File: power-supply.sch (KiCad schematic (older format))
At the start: 16 parts, among them J13 USB_A, U11 BA33BC0FP-E2, U13 LM2990SX-5.0, U14 BA50BC0FP-E2

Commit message: Minor fixes and cleanups
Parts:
- C18: value 22uF -> 330uF/LOW_ESR; footprint Capacitor_SMD:CP_Elec_6.3x5.4 -> Capacitor_SMD:CP_Elec_6.3x7.7
- C19, C25, C28: value 1uF -> 10uF
- C24: value 33uF/LOW_ESR -> 100uF
- C26: footprint Capacitor_SMD:CP_Elec_6.3x5.4 -> Capacitor_SMD:CP_Elec_6.3x7.7
- C29: footprint Capacitor_SMD:CP_Elec_6.3x5.4 -> Capacitor_SMD:CP_Elec_6.3x5.8
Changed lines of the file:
@@
 P 1950 3700
 F 0 "C19" H 1960 3770 50  0000 L CNN
-F 1 "1uF" H 1960 3620 50  0000 L CNN
+F 1 "10uF" H 1960 3620 50  0000 L CNN
 F 2 "Capacitor_SMD:C_0805_2012Metric_Pad1.18x1.45mm_HandSolder" H 1950 3700 50  0001 C CNN
 F 3 "" H 1950 3700 50  0001 C CNN
@@
 P 2750 3700
 F 0 "C18" H 2838 3746 50  0000 L CNN
-F 1 "22uF" H 2838 3655 50  0000 L CNN
-F 2 "Capacitor_SMD:CP_Elec_6.3x5.4" H 2750 3700 50  0001 C CNN
+F 1 "330uF/LOW_ESR" H 2838 3655 50  0000 L CNN
+F 2 "Capacitor_SMD:CP_Elec_6.3x7.7" H 2750 3700 50  0001 C CNN
 F 3 "~" H 2750 3700 50  0001 C CNN
 	1    2750 3700
@@
 F 0 "C26" H 9688 4246 50  0000 L CNN
 F 1 "330uF/LOW_ESR" H 9688 4155 50  0000 L CNN
-F 2 "Capacitor_SMD:CP_Elec_6.3x5.4" H 9600 4200 50  0001 C CNN
+F 2 "Capacitor_SMD:CP_Elec_6.3x7.7" H 9600 4200 50  0001 C CNN
 F 3 "~" H 9600 4200 50  0001 C CNN
 	1    9600 4200
@@
 P 4250 3550
 F 0 "C24" V 4350 3500 50  0000 L CNN
-F 1 "33uF/LOW_ESR" V 4450 3100 50  0000 L CNN
+F 1 "100uF" V 4150 3450 50  0000 L CNN
 F 2 "Capacitor_SMD:CP_Elec_6.3x5.4" H 4250 3550 50  0001 C CNN
 F 3 "~" H 4250 3550 50  0001 C CNN
@@
 F 0 "C29" H 8288 4346 50  0000 L CNN
 F 1 "330uF/LOW_ESR" H 8288 4255 50  0000 L CNN
-F 2 "Capacitor_SMD:CP_Elec_6.3x5.4" H 8200 4300 50  0001 C CNN
+F 2 "Capacitor_SMD:CP_Elec_6.3x5.8" H 8200 4300 50  0001 C CNN
 F 3 "~" H 8200 4300 50  0001 C CNN
 	1    8200 4300
@@
 P 8800 4200
 F 0 "C25" H 8810 4270 50  0000 L CNN
-F 1 "1uF" H 8810 4120 50  0000 L CNN
+F 1 "10uF" H 8810 4120 50  0000 L CNN
 F 2 "Capacitor_SMD:C_0805_2012Metric_Pad1.18x1.45mm_HandSolder" H 8800 4200 50  0001 C CNN
 F 3 "" H 8800 4200 50  0001 C CNN
@@
 P 7200 4300
 F 0 "C28" H 7210 4370 50  0000 L CNN
-F 1 "1uF" H 7210 4220 50  0000 L CNN
+F 1 "10uF" H 7210 4220 50  0000 L CNN
 F 2 "Capacitor_SMD:C_0805_2012Metric_Pad1.18x1.45mm_HandSolder" H 7200 4300 50  0001 C CNN
 F 3 "" H 7200 4300 50  0001 C CNN

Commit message: Onboard FPGA, passthroughs and a lot of other stuff
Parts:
- removed J13: USB_A, Connector_USB:USB_A_Molex_67643_Horizontal, symbol Connector:USB_A
- added C30, C31, C32, C33, C34, C35, C36, C37, C38, C39: 0.1uF, Capacitor_SMD:C_0603_1608Metric_Pad1.08x0.95mm_HandSolder, symbol bkm-68x-simple-rescue:C_Small
- added C56, C57, C59: 0.1uF, Capacitor_SMD:C_0805_2012Metric_Pad1.18x1.45mm_HandSolder, symbol bkm-68x-simple-rescue:C_Small
- added C58: 100uF, Capacitor_SMD:CP_Elec_6.3x5.4, symbol Device:CP_Small
- added U15: 10M08SC, Package_QFP:EQFP-144-1EP_20x20mm_P0.5mm_EP8.93x8.7mm_ThermalVias, symbol bkm-68x-simple-rescue:10M08SC-FPGA_Intel
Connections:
- wire segments 53 -> 84
- no-connect marks 2 -> 0
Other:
- moved on the sheet: C14, C15, C16, C17, C18, C19, C23, C24, U11

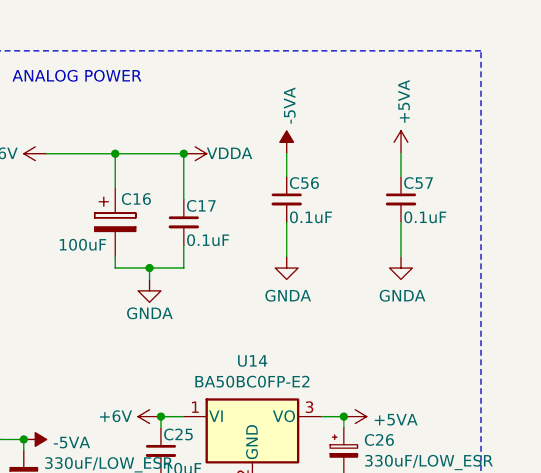
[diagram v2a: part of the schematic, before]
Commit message: Replace ADG1611BRUZ with BCPZ
Should also be compatible with Vishay DG1411EEN-T1-GE4
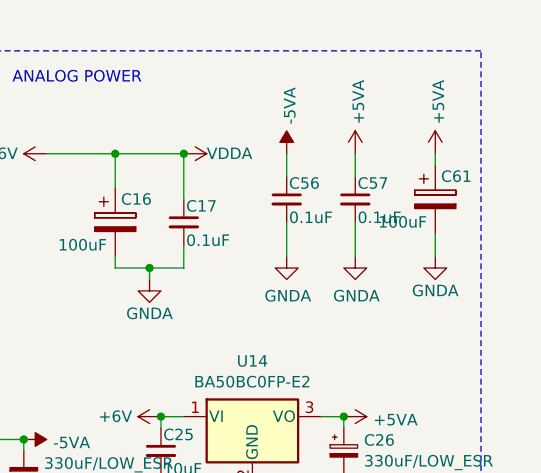
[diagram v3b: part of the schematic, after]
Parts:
- added C61: 100uF, Capacitor_SMD:CP_Elec_6.3x5.3, symbol bkm-68x-simple-rescue:CP
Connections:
- net +5VA: now also C61.1
- net GNDA: now also C61.2
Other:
- moved on the sheet: C57
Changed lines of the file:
@@
 L bkm-68x-simple-rescue:C_Small C57
 U 1 1 60B680F3
-P 9850 3100
-F 0 "C57" H 9860 3170 50  0000 L CNN
-F 1 "0.1uF" H 9860 3020 50  0000 L CNN
-F 2 "Capacitor_SMD:C_0805_2012Metric_Pad1.18x1.45mm_HandSolder" H 9850 3100 50  0001 C CNN
-F 3 "" H 9850 3100 50  0001 C CNN
-	1    9850 3100
+P 9650 3100
+F 0 "C57" H 9660 3170 50  0000 L CNN
+F 1 "0.1uF" H 9660 3020 50  0000 L CNN
+F 2 "Capacitor_SMD:C_0805_2012Metric_Pad1.18x1.45mm_HandSolder" H 9650 3100 50  0001 C CNN
+F 3 "" H 9650 3100 50  0001 C CNN
+	1    9650 3100
 	1    0    0    -1
 $EndComp
@@
 L power:GNDA #PWR0259
 U 1 1 60B680FD
-P 9850 3350
-F 0 "#PWR0259" H 9850 3100 50  0001 C CNN
-F 1 "GNDA" H 9855 3177 50  0000 C CNN
-F 2 "" H 9850 3350 50  0001 C CNN
-F 3 "" H 9850 3350 50  0001 C CNN
-	1    9850 3350
+P 9650 3350
+F 0 "#PWR0259" H 9650 3100 50  0001 C CNN
+F 1 "GNDA" H 9655 3177 50  0000 C CNN
+F 2 "" H 9650 3350 50  0001 C CNN
+F 3 "" H 9650 3350 50  0001 C CNN
+	1    9650 3350
 	1    0    0    -1
 $EndComp
 Wire Wire Line
-	9850 2900 9850 3000
+	9650 2900 9650 3000
 Wire Wire Line
-	9850 3200 9850 3350
+	9650 3200 9650 3350
 $Comp
 L power:+5VA #PWR0260
 U 1 1 60B6D3E9
-P 9850 2900
-F 0 "#PWR0260" H 9850 2750 50  0001 C CNN
-F 1 "+5VA" V 9865 3028 50  0000 L CNN
-F 2 "" H 9850 2900 50  0001 C CNN
-F 3 "" H 9850 2900 50  0001 C CNN
-	1    9850 2900
+P 9650 2900
+F 0 "#PWR0260" H 9650 2750 50  0001 C CNN
+F 1 "+5VA" V 9665 3028 50  0000 L CNN
+F 2 "" H 9650 2900 50  0001 C CNN
+F 3 "" H 9650 2900 50  0001 C CNN
+	1    9650 2900
 	1    0    0    -1
 $EndComp
@@
 	1    0    0    -1
 $EndComp
+$Comp
+L bkm-68x-simple-rescue:CP C61
+U 1 1 60B0E14C
+P 10000 3100
+F 0 "C61" H 10025 3200 50  0000 L CNN
+F 1 "100uF" H 9750 3000 50  0000 L CNN
+F 2 "Capacitor_SMD:CP_Elec_6.3x5.3" H 10038 2950 50  0001 C CNN
+F 3 "" H 10000 3100 50  0001 C CNN
+	1    10000 3100
+	1    0    0    -1
+$EndComp
+$Comp
+L power:GNDA #PWR0269
+U 1 1 60B0EAFC
+P 10000 3350
+F 0 "#PWR0269" H 10000 3100 50  0001 C CNN
+F 1 "GNDA" H 10000 3200 50  0000 C CNN
+F 2 "" H 10000 3350 50  0001 C CNN
+F 3 "" H 10000 3350 50  0001 C CNN
+	1    10000 3350
+	1    0    0    -1
+$EndComp
+Wire Wire Line
+	10000 2900 10000 2950
+Wire Wire Line
+	10000 3250 10000 3350
+$Comp
+L power:+5VA #PWR?
+U 1 1 60B17D98
+P 10000 2900
+F 0 "#PWR?" H 10000 2750 50  0001 C CNN
+F 1 "+5VA" V 10015 3028 50  0000 L CNN
+F 2 "" H 10000 2900 50  0001 C CNN
+F 3 "" H 10000 2900 50  0001 C CNN
+	1    10000 2900
+	1    0    0    -1
+$EndComp

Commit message: Revision D1
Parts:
- added J18: Conn_01x02_Male, Connector_PinHeader_2.54mm:PinHeader_1x02_P2.54mm_Vertical, symbol Connector:Conn_01x02_Male
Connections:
- net GNDD: now also J18.2 (Pin_2)
- net STBY_5V: now also J18.1 (Pin_1)
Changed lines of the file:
@@
 	1    0    0    -1
 $EndComp
+$Comp
+L Connector:Conn_01x02_Male J18
+U 1 1 60F3F876
+P 2250 3550
+F 0 "J18" H 2358 3731 50  0000 C CNN
+F 1 "Conn_01x02_Male" H 2358 3640 50  0000 C CNN
+F 2 "Connector_PinHeader_2.54mm:PinHeader_1x02_P2.54mm_Vertical" H 2250 3550 50  0001 C CNN
+F 3 "~" H 2250 3550 50  0001 C CNN
+	1    2250 3550
+	1    0    0    -1
+$EndComp
+Text GLabel 2450 3550 2    50   Input ~ 0
+STBY_5V
+$Comp
+L power:GNDD #PWR0279
+U 1 1 60F4055F
+P 2450 3650
+F 0 "#PWR0279" H 2450 3400 50  0001 C CNN
+F 1 "GNDD" V 2450 3450 50  0000 C CNN
+F 2 "" H 2450 3650 50  0001 C CNN
+F 3 "" H 2450 3650 50  0001 C CNN
+	1    2450 3650
+	0    -1   -1   0
+$EndComp
 $EndSCHEMATC

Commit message: Rev. E
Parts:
- added C66, C67: 2.2uF, Capacitor_SMD:C_0805_2012Metric_Pad1.18x1.45mm_HandSolder, symbol bkm-68x-simple-rescue:C_Small
- added C68, C70: 10uF, Capacitor_SMD:C_0805_2012Metric_Pad1.18x1.45mm_HandSolder, symbol bkm-68x-simple-rescue:C_Small
- added R85: 22,1K 0,1%, Resistor_SMD:R_0805_2012Metric_Pad1.20x1.40mm_HandSolder, symbol Device:R_Small
- added R86: 82,5K 0.1%, Resistor_SMD:R_0805_2012Metric_Pad1.20x1.40mm_HandSolder, symbol Device:R_Small
- added U18: TPS72301, Package_TO_SOT_SMD:SOT-23-5, symbol tps723xx:TPS723xx
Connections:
- net +5VA: now also C68.1, C70.1
- net GNDA: now also C66.2, C67.2, C68.2, C70.2, R86.2, U18.1 (GND)
- net VSSA: now also C66.1, U18.2 (IN), U18.3 (EN)
- new net: R85.2, R86.1, U18.4 (FB/NR)
- new net -1.5V: C67.1, R85.1, U18.5 (OUT)
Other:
- moved on the sheet: C14, C15, C16, C17, C25, C26, C28, C29, C56, C57, C61, U13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

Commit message: Rev. E1
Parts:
- removed C66, C67: 2.2uF, Capacitor_SMD:C_0805_2012Metric_Pad1.18x1.45mm_HandSolder, symbol bkm-68x-simple-rescue:C_Small
- removed R85: 22,1K 0,1%, Resistor_SMD:R_0805_2012Metric_Pad1.20x1.40mm_HandSolder, symbol Device:R_Small
- removed R86: 82,5K 0.1%, Resistor_SMD:R_0805_2012Metric_Pad1.20x1.40mm_HandSolder, symbol Device:R_Small
- removed U18: TPS72301, Package_TO_SOT_SMD:SOT-23-5, symbol tps723xx:TPS723xx
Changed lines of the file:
@@
 	7150 4550 7150 800
-$Comp
-L tps723xx:TPS723xx U18
-U 1 1 611C3B37
-P 8900 3650
-F 0 "U18" H 8900 4115 50  0000 C CNN
-F 1 "TPS72301" H 8900 4024 50  0000 C CNN
-F 2 "Package_TO_SOT_SMD:SOT-23-5" H 8750 3700 50  0001 C CNN
-F 3 "" H 8750 3700 50  0001 C CNN
-	1    8900 3650
-	1    0    0    -1
-$EndComp
-Text GLabel 8250 3450 0    60   Input ~ 0
--6V
-$Comp
-L power:GNDA #PWR0153
-U 1 1 611C7EAE
-P 8900 4200
-F 0 "#PWR0153" H 8900 3950 50  0001 C CNN
-F 1 "GNDA" H 8905 4027 50  0000 C CNN
-F 2 "" H 8900 4200 50  0001 C CNN
-F 3 "" H 8900 4200 50  0001 C CNN
-	1    8900 4200
-	1    0    0    -1
-$EndComp
-Wire Wire Line
-	8900 4200 8900 4150
-Wire Wire Line
-	8350 4150 8900 4150
-Connection ~ 8900 4150
-Wire Wire Line
-	8250 3450 8350 3450
-$Comp
-L bkm-68x-simple-rescue:C_Small C66
-U 1 1 611CD71D
-P 8350 3950
-F 0 "C66" H 8360 4020 50  0000 L CNN
-F 1 "2.2uF" H 8360 3870 50  0000 L CNN
-F 2 "Capacitor_SMD:C_0805_2012Metric_Pad1.18x1.45mm_HandSolder" H 8350 3950 50  0001 C CNN
-F 3 "" H 8350 3950 50  0001 C CNN
-	1    8350 3950
-	1    0    0    -1
-$EndComp
-Wire Wire Line
-	8350 3850 8350 3700
-Connection ~ 8350 3450
-Wire Wire Line
-	8350 3450 8450 3450
-Wire Wire Line
-	8350 4050 8350 4150
-$Comp
-L bkm-68x-simple-rescue:C_Small C67
-U 1 1 611D349D
-P 9850 4000
-F 0 "C67" H 9860 4070 50  0000 L CNN
-F 1 "2.2uF" H 9860 3920 50  0000 L CNN
-F 2 "Capacitor_SMD:C_0805_2012Metric_Pad1.18x1.45mm_HandSolder" H 9850 4000 50  0001 C CNN
-F 3 "" H 9850 4000 50  0001 C CNN
-	1    9850 4000
-	1    0    0    -1
-$EndComp
-Wire Wire Line
-	9350 3450 9400 3450
-Wire Wire Line
-	8350 3700 8450 3700
-Connection ~ 8350 3700
-Wire Wire Line
-	8350 3700 8350 3450
-$Comp
-L Device:R_Small R85
-U 1 1 611E03CA
-P 9400 3550
-F 0 "R85" H 9459 3596 50  0000 L CNN
-F 1 "22,1K 0,1%" H 9459 3505 50  0000 L CNN
-F 2 "Resistor_SMD:R_0805_2012Metric_Pad1.20x1.40mm_HandSolder" H 9400 3550 50  0001 C CNN
-F 3 "~" H 9400 3550 50  0001 C CNN
-	1    9400 3550
-	1    0    0    -1
-$EndComp
-$Comp
-L Device:R_Small R86
-U 1 1 611E09D0
-P 9400 3850
-F 0 "R86" H 9459 3896 50  0000 L CNN
-F 1 "82,5K 0.1%" H 9459 3805 50  0000 L CNN
-F 2 "Resistor_SMD:R_0805_2012Metric_Pad1.20x1.40mm_HandSolder" H 9400 3850 50  0001 C CNN
-F 3 "~" H 9400 3850 50  0001 C CNN
-	1    9400 3850
-	1    0    0    -1
-$EndComp
-Wire Wire Line
-	8900 4150 9400 4150
-Wire Wire Line
-	9850 4150 9850 4100
-Wire Wire Line
-	9400 3450 9850 3450
-Wire Wire Line
-	9850 3450 9850 3900
-Connection ~ 9400 3450
-Wire Wire Line
-	9400 3650 9400 3700
-Wire Wire Line
-	9350 3700 9400 3700
-Connection ~ 9400 3700
-Wire Wire Line
-	9400 3700 9400 3750
-Wire Wire Line
-	9400 3950 9400 4150
-Connection ~ 9400 4150
-Wire Wire Line
-	9400 4150 9850 4150
-Text GLabel 9850 3450 2    50   Input ~ 0
--1.5V
 $Comp
 L bkm-68x-simple-rescue:C_Small C68

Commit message: Rev. F1
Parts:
- removed C18: 330uF/LOW_ESR, Capacitor_SMD:CP_Elec_6.3x7.7, symbol Device:CP_Small
- removed U11: BA33BC0FP-E2, Package_TO_SOT_SMD:TO-252-3_TabPin2, symbol Regulator_Linear:SPX2920U-3.3_TO220
- removed U15: 10M08SC, Package_QFP:EQFP-144-1EP_20x20mm_P0.5mm_EP8.93x8.7mm_ThermalVias, symbol bkm-68x-simple-rescue:10M08SC-FPGA_Intel
- added C111, C112, C113, C114: 1uF, Capacitor_SMD:C_0805_2012Metric_Pad1.18x1.45mm_HandSolder, symbol bkm-68x-simple-rescue:C_Small
- added C18: 100uF, Capacitor_SMD:CP_Elec_6.3x5.3, symbol bkm-68x-simple-rescue:CP
- added C811, C812: 0.1uF, Capacitor_SMD:C_0603_1608Metric_Pad1.08x0.95mm_HandSolder, symbol bkm-68x-simple-rescue:C_Small
- added R101: 10K, Resistor_SMD:R_0805_2012Metric_Pad1.20x1.40mm_HandSolder, symbol Device:R_Small
- added U101: NCV8164ASN120T1G, Package_SO:TSOP-5_1.65x3.05mm_P0.95mm, symbol ldo-en-pg:NCV8164
- added U102: BD33HC0WEFJ-E2, Package_SO:HTSOP-8-1EP_3.9x4.9mm_P1.27mm_EP2.4x3.2mm_ThermalVias, symbol ldo-en-pg:BDxxHC0WEFJ
- added U801: T8Q144, Package_QFP:TQFP-144_20x20mm_P0.5mm, symbol bkm-68x-simple-rescue:T8Q144-Efinix_FPGA
- C19: value 10uF -> 0.1uF
- renumbered C30 to C801, C31 to C802, C32 to C803, C33 to C804, C34 to C805, C35 to C806, C36 to C807, C37 to C808, C38 to C809, C39 to C810
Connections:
- net +3V3: now also C113.1, U102.1 (VOUT), U102.2 (VOUT_S); no longer C801.1, C802.1, C803.1, C804.1, C805.1, C806.1, C807.1, C808.1, C809.1, C810.1
- net +5VA: now also C19.1, C18.1
- net GNDA: now also C19.2, C18.2
- net GNDD: now also C111.2, C112.2, C113.2, C114.2, C811.2, C812.2, U101.2 (GND), U102.3 (GND), U102.9 (EP), U801.1 (GND), U801.104 (GND), U801.108 (GND), U801.120 (GND), U801.121 (GND), U801.126 (GND), U801.127 (GND), U801.129 (GND), U801.133 (GND), U801.37 (GND), U801.44 (GND), U801.5 (GND), U801.50 (GND), U801.64 (GND), U801.9 (GND), U801.94 (GND); no longer C19.2
- net STBY_5V: now also C111.1, C114.1, R101.1, U101.1 (VIN), U101.3 (EN), U102.8 (VIN); no longer C19.1
- new net +1V2: C112.1, C801.1, C802.1, C803.1, C804.1, C805.1, C806.1, C807.1, C808.1, C809.1, C810.1, C811.1, C812.1, U101.5 (VOUT), U801.107 (VCCA_TR), U801.125 (VCC), U801.128 (VCC), U801.13 (VCC), U801.130 (VCC), U801.2 (VCCA_TL), U801.22 (VCC), U801.49 (VCC), U801.57 (VCC), U801.73 (VCCA_BR), U801.85 (VCC), U801.96 (VCC)
- new net VCORE_GOOD: R101.2, U101.4 (PGOOD), U102.5 (EN)
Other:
- moved on the sheet: C23, C24, C58, C59, C801, C802, C803, C804, C805, C806, C807, C808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
